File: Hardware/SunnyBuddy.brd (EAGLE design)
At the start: 47 x 47 mm, 34 parts, among them J1 5.5x2.1mm Barrel, J3 POWER_JACKPTH, J5 M02PTH, J6 M023.5MM, J7 M023.5MM, J8 M023.5MM, U1 LT3652

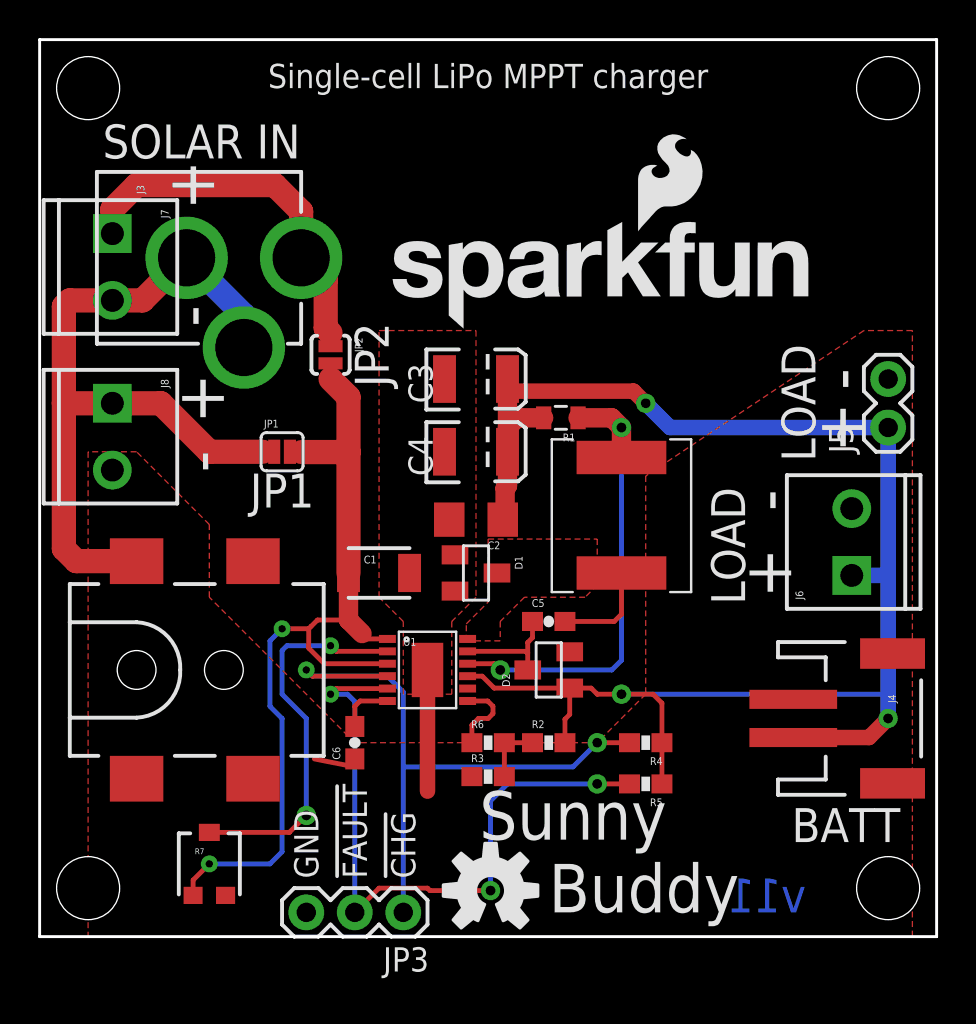
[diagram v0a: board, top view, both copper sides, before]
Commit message: Add current sense jumper, set V node, Fritzing
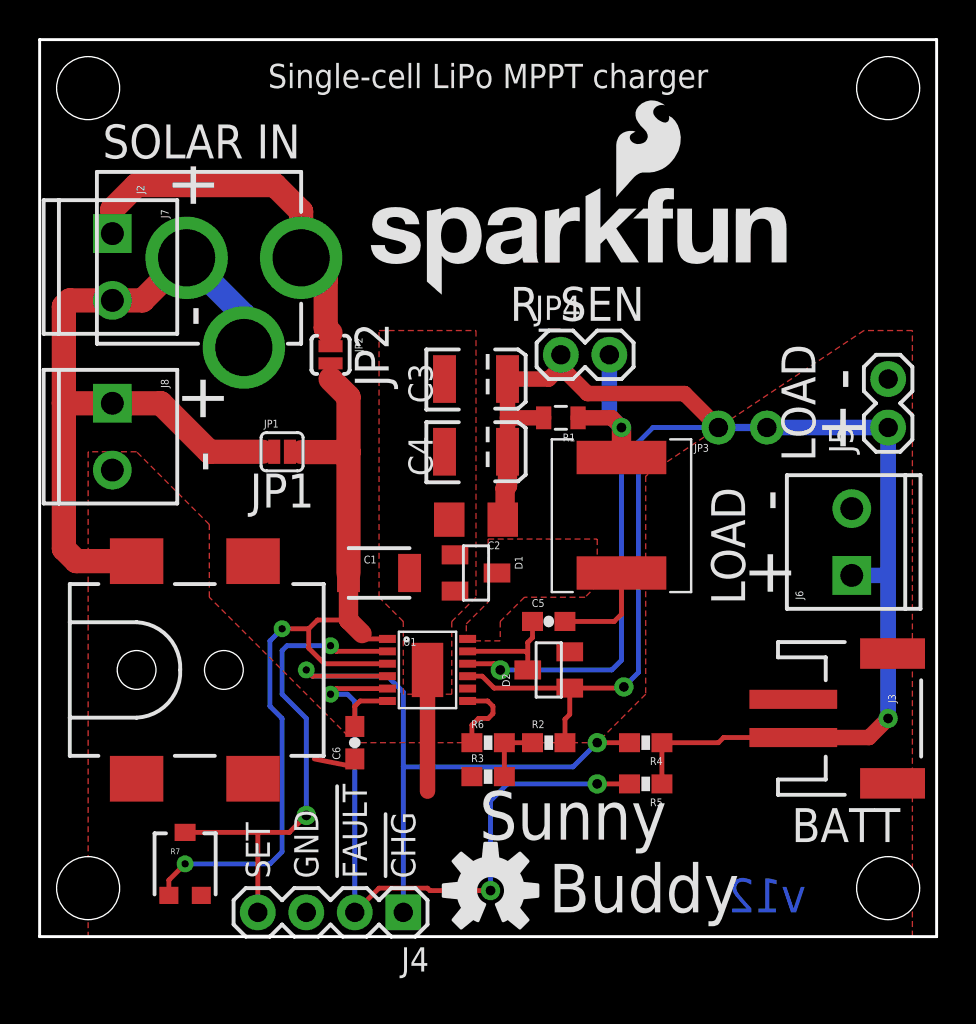
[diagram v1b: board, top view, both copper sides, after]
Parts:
- added J2: POWER_JACKPTH, SparkFun-Connectors:POWER_JACK_PTH
- added JP4: R_SEN, SparkFun-Connectors:1X02
- J3: value POWER_JACKPTH -> (none); device SparkFun-Connectors:POWER_JACK_PTH -> SparkFun-Connectors:JST-2-SMD
- J4: device SparkFun-Connectors:JST-2-SMD -> SparkFun-Connectors:1X04
- JP3: value (none) -> JUMPER-PTH-2-NC; device SparkFun-Connectors:1X03 -> SparkFun-Passives:PTH-JUMPER-NC_BOTTOM_NO_SILK
- moved J3 49.5 mm to (43.2, 11.4)
- moved JP3 31.0 mm to (36.8, 26.7), turned to 0 degrees
- moved J4 26.2 mm to (19.1, 1.27), turned to 180 degrees
- moved LOGO1 2.11 mm to (16.6, 33.5)
- moved R7 1.27 mm to (7.62, 3.81)
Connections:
- new net SET: J4.4, R7.2, U1.2
- net !CHRG: now also J4.1; no longer JP3.1
- net !FAULT: now also J4.2; no longer JP3.2
- net GND: now also J3.1, J3.NC1, J3.NC2, J4.3; no longer J4.1, J4.NC1, J4.NC2, JP3.3
- net N$4: now also C2.1, C3.A, C4.A, D2.1, JP3.1, JP4.1, R1.2, R2.2, U1.9; no longer R7.2, U1.2
- net N$8: now also J2.GND, J2.GNDBREAK; no longer J3.GND, J3.GNDBREAK
- net SENSE: now also JP4.2
- net SFSASDF: now also J2.PWR; no longer J3.PWR
- net V_BATT: now also J3.2, JP3.2; no longer C2.1, C3.A, C4.A, D2.1, J4.2, R1.2, R2.2, U1.9
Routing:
- net V_BATT: track 85.1 -> 38.1 mm, vias 3 -> 1
- net N$4: track 20.4 -> 51.9 mm, vias 2 -> 1
- net SET: track 0.00 -> 25.8 mm, vias 0 -> 2
- net SENSE: track 24.7 -> 28.7 mm
- net VIN: track 46.8 -> 48.1 mm
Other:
- board text added: "R_SEN"
- board text added: "SET"
- board text added: "v12"
- board text removed: "v11"

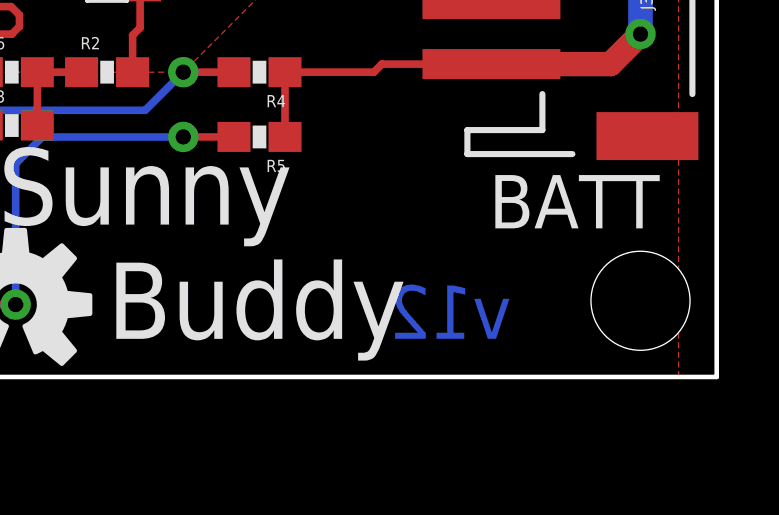
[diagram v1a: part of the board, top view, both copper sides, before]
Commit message: Changes to silk, only, for production
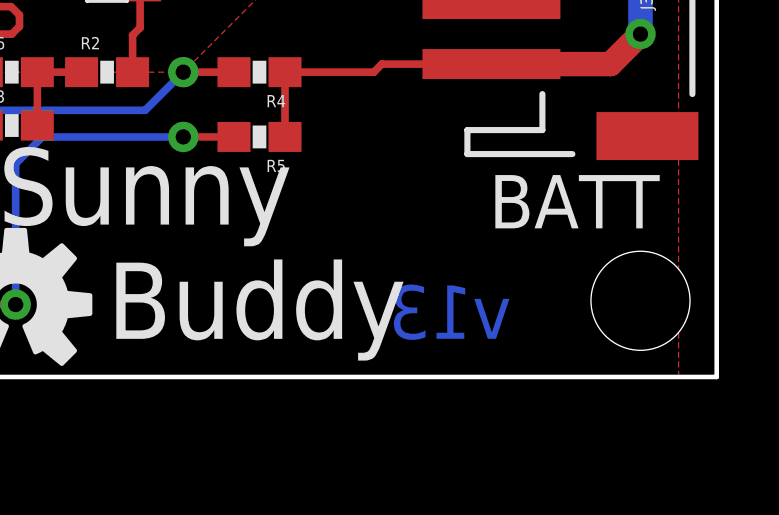
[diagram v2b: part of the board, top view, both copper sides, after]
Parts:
- added LOGO3: OSHW-LOGOS, SparkFun-Aesthetics:OSHW-LOGO-S
- added LOGO4: SFE_LOGO_NAME_FLAME.3_INCH, SparkFun-Aesthetics:SFE_LOGO_NAME_FLAME_.3
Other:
- board text added: "!CHARGE"
- board text added: "I_SEN"
- board text added: "v13"
- board text removed: "v12"
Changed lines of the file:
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@@
 <grid distance="0.05" unitdist="inch" unit="inch" style="lines" multiple="1" display="yes" altdistance="0.005" altunitdist="inch" altunit="inch"/>
 <layers>
-<layer number="1" name="Top" color="4" fill="1" visible="yes" active="yes"/>
+<layer number="1" name="Top" color="4" fill="1" visible="no" active="yes"/>
 <layer number="2" name="Route2" color="1" fill="3" visible="no" active="yes"/>
 <layer number="15" name="Route15" color="4" fill="6" visible="no" active="yes"/>
@@
 <layer number="19" name="Unrouted" color="6" fill="1" visible="yes" active="yes"/>
 <layer number="20" name="Dimension" color="15" fill="1" visible="yes" active="yes"/>
-<layer number="21" name="tPlace" color="16" fill="1" visible="yes" active="yes"/>
+<layer number="21" name="tPlace" color="16" fill="1" visible="no" active="yes"/>
 <layer number="22" name="bPlace" color="14" fill="1" visible="yes" active="yes"/>
-<layer number="23" name="tOrigins" color="15" fill="1" visible="yes" active="yes"/>
+<layer number="23" name="tOrigins" color="15" fill="1" visible="no" active="yes"/>
 <layer number="24" name="bOrigins" color="15" fill="1" visible="yes" active="yes"/>
 <layer number="25" name="tNames" color="7" fill="1" visible="no" active="yes"/>
@@
 <layer number="43" name="vRestrict" color="2" fill="10" visible="no" active="yes"/>
 <layer number="44" name="Drills" color="7" fill="1" visible="no" active="yes"/>
-<layer number="45" name="Holes" color="7" fill="1" visible="yes" active="yes"/>
+<layer number="45" name="Holes" color="7" fill="1" visible="no" active="yes"/>
 <layer number="46" name="Milling" color="3" fill="1" visible="no" active="yes"/>
-<layer number="51" name="tDocu" color="6" fill="1" visible="yes" active="yes"/>
+<layer number="51" name="tDocu" color="6" fill="1" visible="no" active="yes"/>
 <layer number="52" name="bDocu" color="7" fill="1" visible="no" active="yes"/>
 <layer number="3" name="Route3" color="4" fill="3" visible="no" active="no"/>
@@
 <layer number="108" name="tplace-old" color="10" fill="1" visible="no" active="no"/>
 <layer number="109" name="ref-old" color="11" fill="1" visible="no" active="no"/>
-<layer number="110" name="fp0" color="7" fill="1" visible="no" active="yes"/>
-<layer number="111" name="LPC17xx" color="7" fill="1" visible="no" active="yes"/>
-<layer number="112" name="tSilk" color="7" fill="1" visible="no" active="yes"/>
-<layer number="113" name="IDFDebug" color="4" fill="1" visible="no" active="yes"/>
+<layer number="110" name="fp0" color="7" fill="1" visible="no" active="no"/>
+<layer number="111" name="LPC17xx" color="7" fill="1" visible="no" active="no"/>
+<layer number="112" name="tSilk" color="7" fill="1" visible="no" active="no"/>
+<layer number="113" name="IDFDebug" color="4" fill="1" visible="no" active="no"/>
 <layer number="116" name="Patch_BOT" color="9" fill="4" visible="no" active="no"/>
 <layer number="121" name="_tsilk" color="7" fill="1" visible="no" active="no"/>
 <layer number="122" name="_bsilk" color="7" fill="1" visible="no" active="no"/>
-<layer number="123" name="tTestmark" color="7" fill="1" visible="no" active="yes"/>
-<layer number="124" name="bTestmark" color="7" fill="1" visible="no" active="yes"/>
+<layer number="123" name="tTestmark" color="7" fill="1" visible="no" active="no"/>
+<layer number="124" name="bTestmark" color="7" fill="1" visible="no" active="no"/>
 <layer number="125" name="_tNames" color="7" fill="1" visible="no" active="no"/>
-<layer number="126" name="_bNames" color="7" fill="1" visible="no" active="yes"/>
-<layer number="127" name="_tValues" color="7" fill="1" visible="no" active="yes"/>
-<layer number="128" name="_bValues" color="7" fill="1" visible="no" active="yes"/>
-<layer number="131" name="tAdjust" color="7" fill="1" visible="no" active="yes"/>
-<layer number="132" name="bAdjust" color="7" fill="1" visible="no" active="yes"/>
+<layer number="126" name="_bNames" color="7" fill="1" visible="no" active="no"/>
+<layer number="127" name="_tValues" color="7" fill="1" visible="no" active="no"/>
+<layer number="128" name="_bValues" color="7" fill="1" visible="no" active="no"/>
+<layer number="131" name="tAdjust" color="7" fill="1" visible="no" active="no"/>
+<layer number="132" name="bAdjust" color="7" fill="1" visible="no" active="no"/>
 <layer number="144" name="Drill_legend" color="7" fill="1" visible="no" active="no"/>
 <layer number="151" name="HeatSink" color="7" fill="1" visible="no" active="no"/>
-<layer number="152" name="_bDocu" color="7" fill="1" visible="no" active="yes"/>
+<layer number="152" name="_bDocu" color="7" fill="1" visible="no" active="no"/>
 <layer number="199" name="Contour" color="7" fill="1" visible="no" active="no"/>
 <layer number="200" name="200bmp" color="1" fill="10" visible="no" active="no"/>
@@
 <layer number="223" name="223bmp" color="24" fill="1" visible="no" active="no"/>
 <layer number="224" name="224bmp" color="25" fill="1" visible="no" active="no"/>
-<layer number="248" name="Housing" color="7" fill="1" visible="no" active="yes"/>
-<layer number="249" name="Edge" color="7" fill="1" visible="no" active="yes"/>
+<layer number="248" name="Housing" color="7" fill="1" visible="no" active="no"/>
+<layer number="249" name="Edge" color="7" fill="1" visible="no" active="no"/>
 <layer number="250" name="Descript" color="3" fill="1" visible="no" active="no"/>
 <layer number="251" name="SMDround" color="12" fill="11" visible="no" active="no"/>
@@
 <text x="18.288" y="30.48" size="1.778" layer="21" font="vector" ratio="15" rot="R90" align="bottom-center">JP2</text>
 <text x="82.55" y="-26.67" size="1.778" layer="51" font="vector" ratio="15" align="bottom-center">M. Hord</text>
-<text x="38.1" y="1.27" size="1.778" layer="16" font="vector" ratio="15" rot="MR0" align="bottom-center">v12</text>
+<text x="38.1" y="1.27" size="1.778" layer="16" font="vector" ratio="15" rot="MR0" align="bottom-center">v13</text>
 <text x="3.302" y="40.767" size="1.778" layer="21" font="vector" ratio="15">SOLAR IN</text>
 <text x="40.64" y="24.892" size="1.778" layer="21" font="vector" ratio="15" rot="R90">LOAD</text>
@@
 <text x="11.43" y="3.048" size="1.27" layer="21" font="vector" ratio="15" rot="R90" align="center-left">SET</text>
 <text x="24.638" y="32.258" size="1.778" layer="21" font="vector" ratio="15">R_SEN</text>
+<text x="31.75" y="31.75" size="1.778" layer="22" font="vector" ratio="15" rot="MR0">R_SEN</text>
+<text x="40.64" y="27.94" size="1.778" layer="22" font="vector" ratio="15" rot="MR0">I_SEN</text>
+<text x="11.43" y="2.54" size="1.778" layer="22" font="vector" ratio="15" rot="MR90" align="center-left">SET</text>
+<text x="13.97" y="2.54" size="1.778" layer="22" font="vector" ratio="15" rot="MR90" align="center-left">GND</text>
+<text x="16.51" y="2.54" size="1.778" layer="22" font="vector" ratio="15" rot="MR90" align="center-left">!FAULT</text>
+<text x="19.05" y="2.54" size="1.778" layer="22" font="vector" ratio="15" rot="MR90" align="center-left">!CHARGE</text>
+<text x="22.225" y="44.45" size="1.27" layer="22" font="vector" ratio="15" rot="MR180" align="top-center">Single-cell LiPo MPPT charger</text>
+<text x="30.48" y="6.35" size="2.54" layer="22" font="vector" ratio="15" rot="MR0" align="bottom-center">Sunny</text>
+<text x="34.29" y="2.54" size="2.54" layer="22" font="vector" ratio="15" rot="MR0">Buddy</text>
 </plain>
 <attributes>
@@
 <element name="JP4" library="SparkFun-Connectors" package="1X02" value="R_SEN" x="27.305" y="30.48"/>
 <element name="JP3" library="SparkFun-Passives" package="PTH-JUMPER-NC_BOTTOM_NO_SILK" value="JUMPER-PTH-2-NC" x="36.83" y="26.67"/>
+<element name="LOGO3" library="SparkFun-Aesthetics" package="OSHW-LOGO-S" value="OSHW-LOGOS" x="2.54" y="7.62" rot="MR0"/>
+<element name="LOGO4" library="SparkFun-Aesthetics" package="SFE_LOGO_NAME_FLAME_.3" value="SFE_LOGO_NAME_FLAME.3_INCH" x="40.64" y="15.24" rot="MR0"/>
 </elements>
 <signals>
